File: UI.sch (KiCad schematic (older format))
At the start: 53 parts, among them Q1 2N7002BK, Q2 BS250P, U7 TXB0108

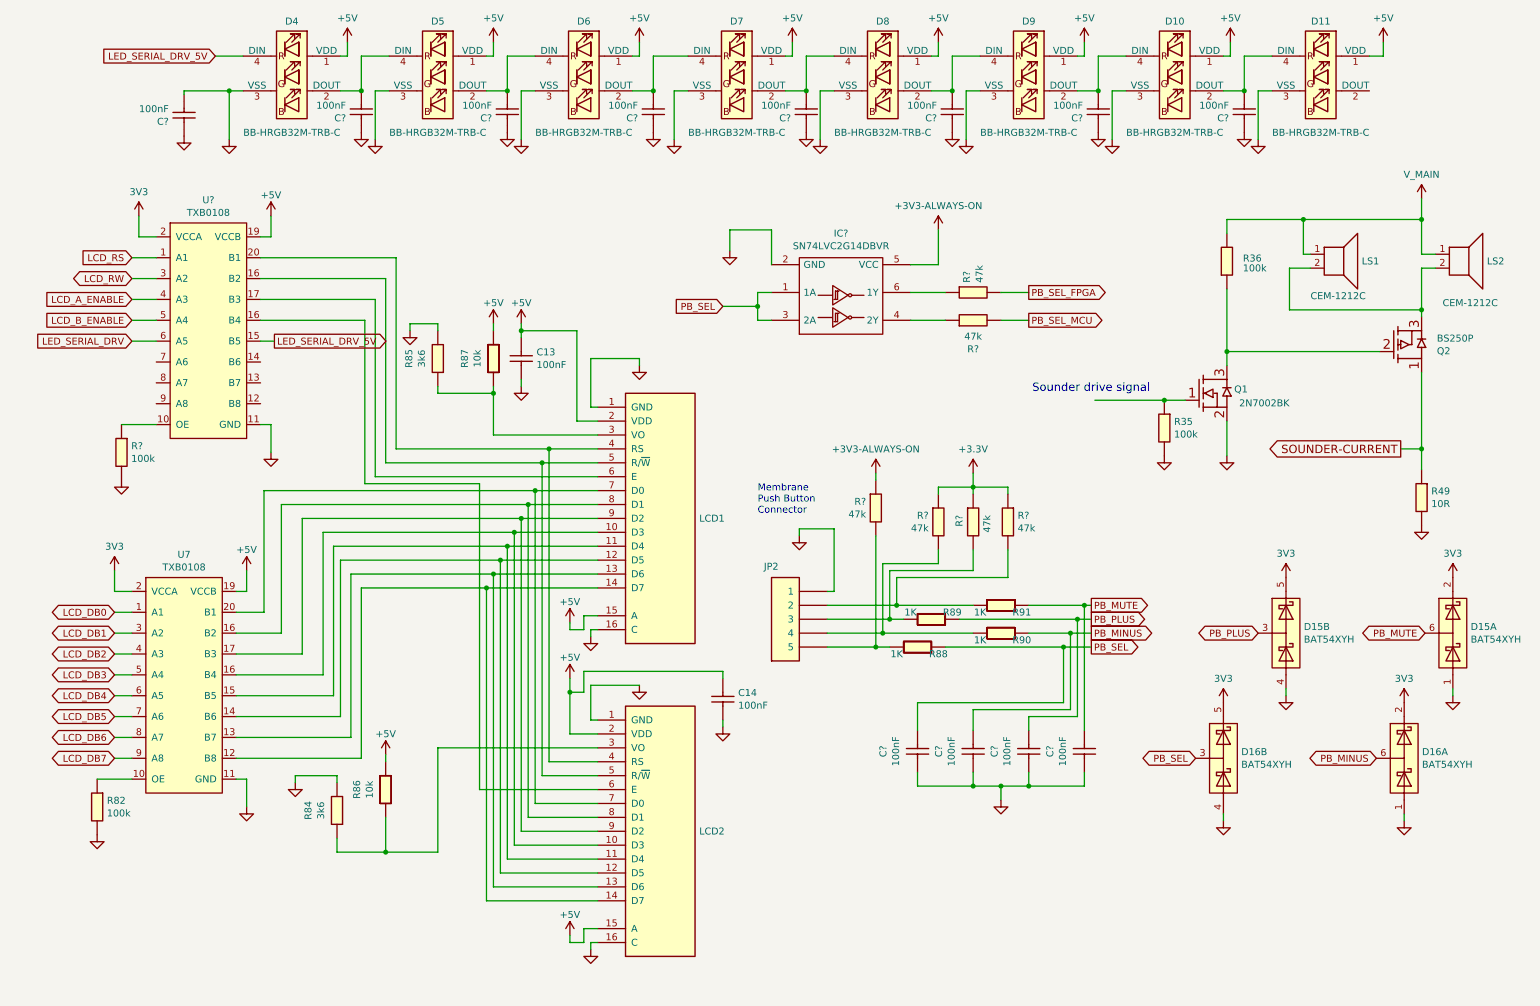
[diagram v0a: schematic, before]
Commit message: Task OEF-623
Split LCD and serial LEDs onto separate sheet as UI too full. Separated the decoupling capacitors from the serial LED for the second time to make schematic clearer. Added 74AHCT1G86 XOR gate to LED drive signal
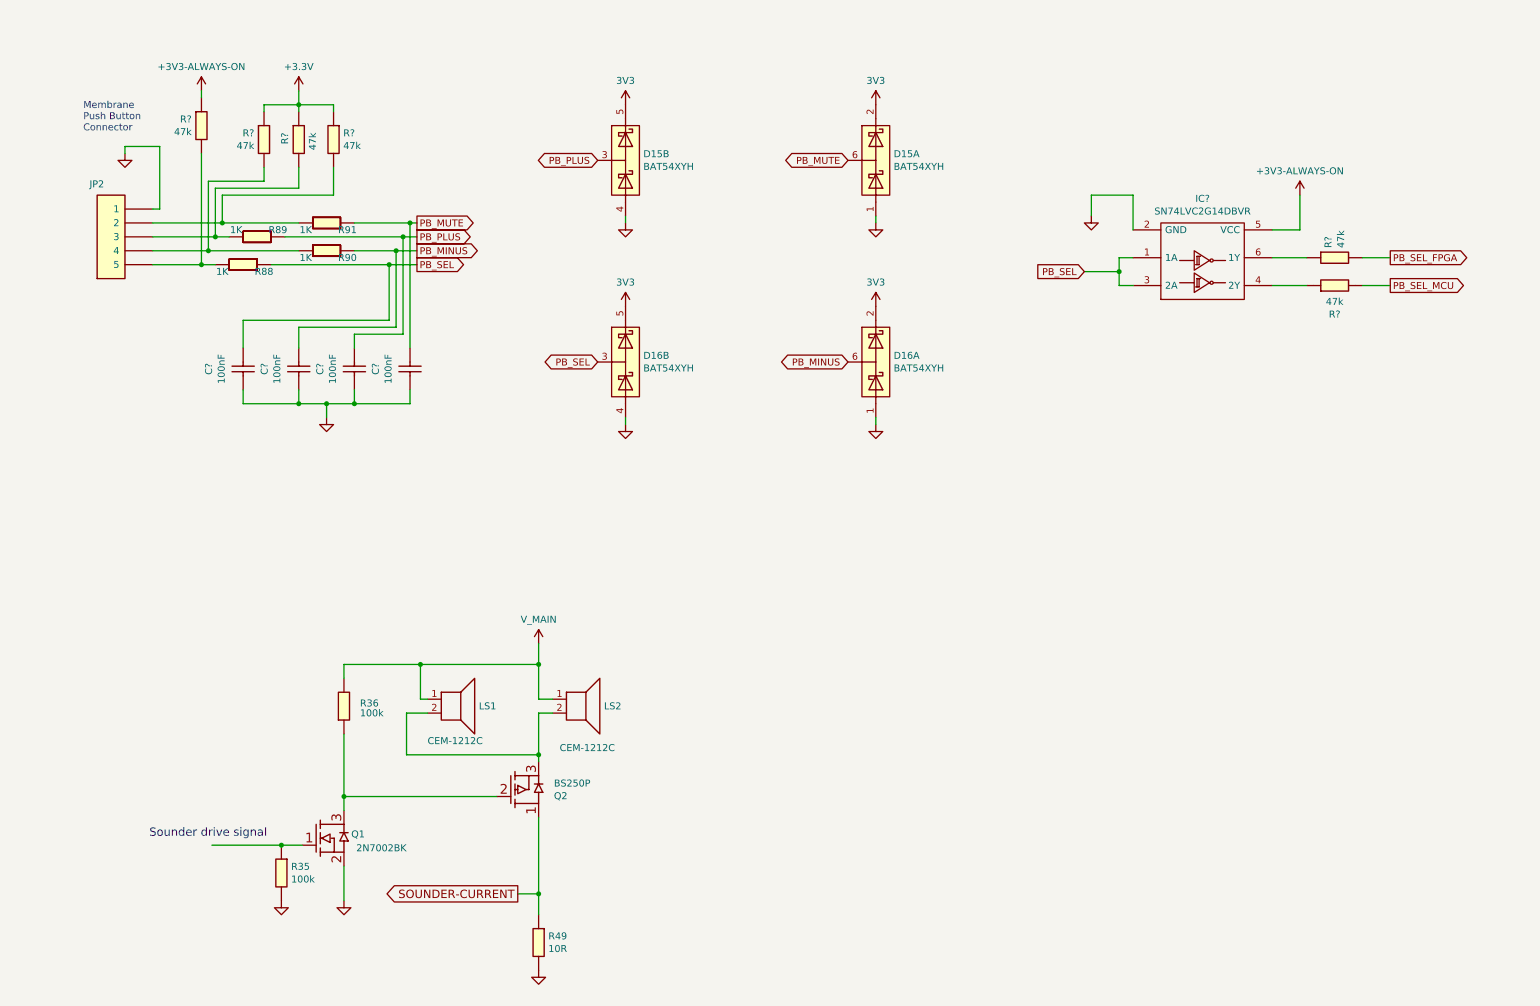
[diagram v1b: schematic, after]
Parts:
- removed C13, C14, C? (x8): 100nF_0603_Ceramic_Capacitor,_10%,_X7R,_25V, symbol OpenVent:100nF_0603_Ceramic_Capacitor,_10%,_X7R,_25V
- removed D10, D11, D4, D5, D6, D7, D8, D9: BB-HRGB32M-TRB-C, symbol OpenVent:BB-HRGB32M-TRB-C
- removed LCD1, LCD2: LCD_MOD_32DIG_16X2_TRANS_YLW_GRN, symbol OpenVent:LCD_MOD_32DIG_16X2_TRANS_YLW_GRN
- removed R82, R?: 100K_0603_Chip_Resistor,_1%,_0.1W, symbol OpenVent:100K_0603_Chip_Resistor,_1%,_0.1W
- removed R84, R85: 3k6_0603_Chip_Resistor,_1%,_0.1W, symbol OpenVent:3k6_0603_Chip_Resistor,_1%,_0.1W
- removed R86, R87: 10k_0603_Chip_Resistor,_1%,_0.1W, symbol OpenVent:10k_0603_Chip_Resistor,_1%,_0.1W
- removed U7, U?: TXB0108, symbol OpenVent:TXB0108
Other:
- moved on the sheet: C?, D15A, D15B, D16A, D16B, IC?, JP2, LS1, LS2, Q1, Q2, R35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

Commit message: Merged Rick's UI
Merged in Rick's copy of UI page (speaker circuit deleted, removing need for separate UI-visual sheet)
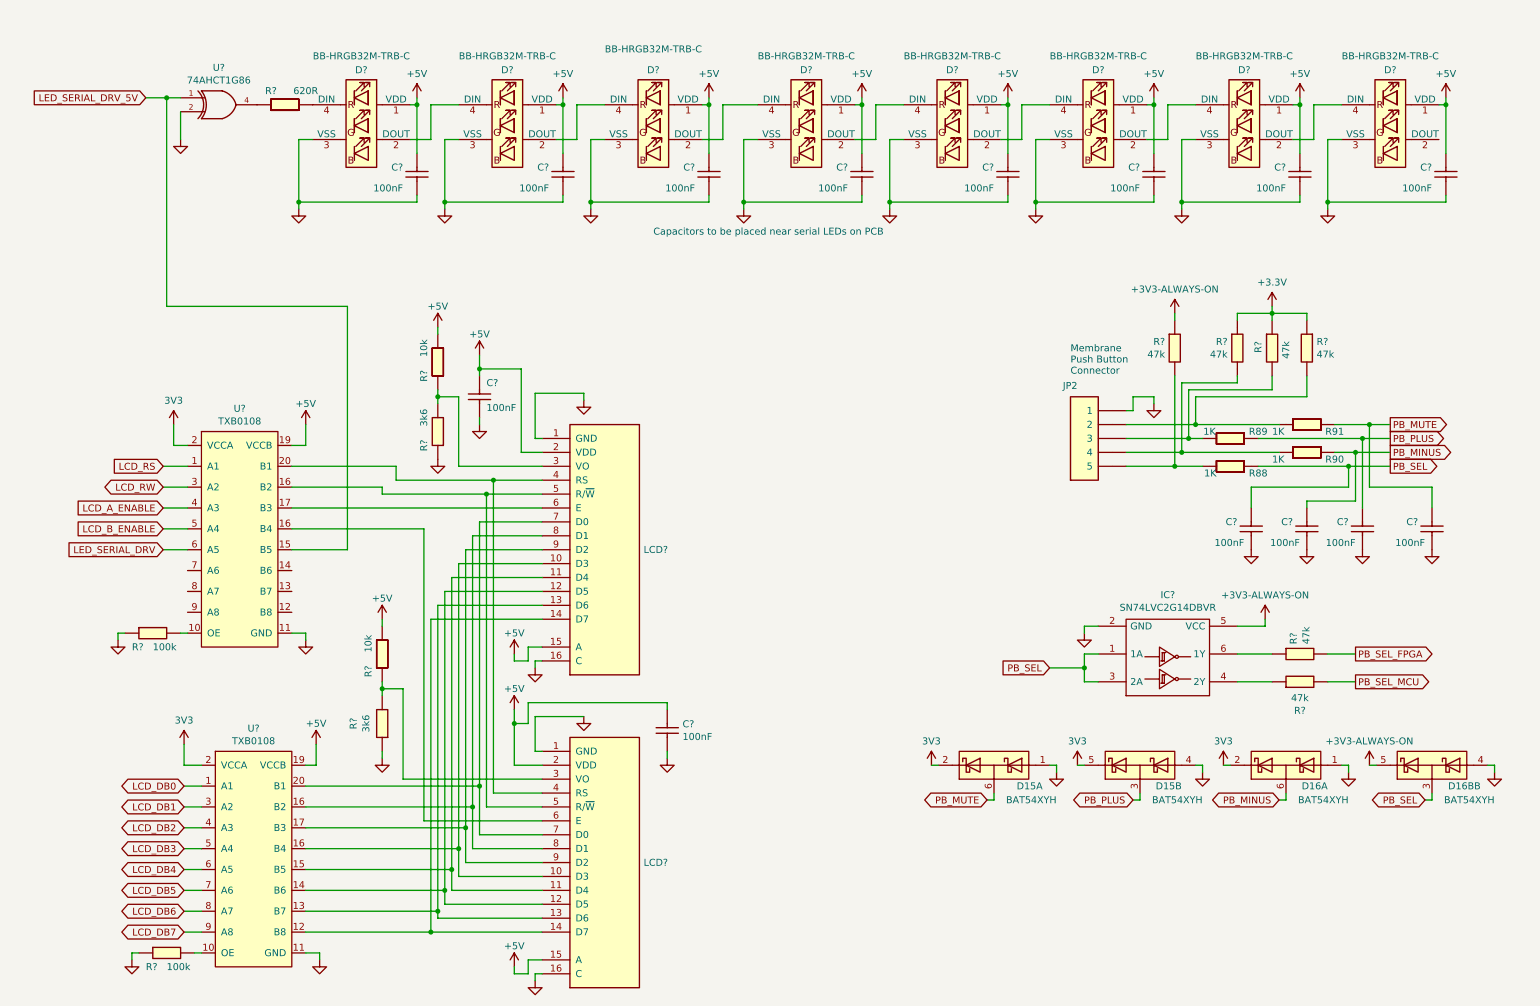
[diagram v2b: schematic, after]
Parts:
- removed C? (x4): 100nF_0603_Ceramic_Capacitor,_10%,_X7R,_25V, symbol OpenVent:100nF_0603_Ceramic_Capacitor,_10%,_X7R,_25V
- removed unit 2 of D16
- removed LS1, LS2: AUDIO_MAGNETIC_INDICATOR, Buzzer_Beeper:Buzzer_12x9.5RM7.6, symbol OpenVent-rescue:AUDIO_MAGNETIC_INDICATOR-Device
- removed Q1: 2N7002BK, Package_TO_SOT_SMD:SOT-23, symbol OpenVent:2N7002BK
- removed Q2: BS250P, symbol OpenVent:BS250P
- removed R35, R36: 100K_0603_Chip_Resistor,_1%,_0.1W, Resistor_SMD:R_0603_1608Metric, symbol OpenVent:100K_0603_Chip_Resistor,_1%,_0.1W
- removed R49: 10R_0603_Chip_Resistor,_1%,_0.1W, Resistor_SMD:R_0603_1608Metric, symbol OpenVent:10R_0603_Chip_Resistor,_1%,_0.1W
- added C? (x14): 100nF_0603_Ceramic_Capacitor,_10%,_X7R,_25V, symbol OpenVent:100nF_0603_Ceramic_Capacitor,_10%,_X7R,_25V
- added D16B: BAT54XYH, symbol OpenVent:BAT54XYH
- added D? (x8): BB-HRGB32M-TRB-C, symbol OpenVent:BB-HRGB32M-TRB-C
- added LCD? (x2): LCD_MOD_32DIG_16X2_TRANS_YLW_GRN, symbol OpenVent:LCD_MOD_32DIG_16X2_TRANS_YLW_GRN
- added R?: R_0603_620R_0.1W_1%, symbol OpenVent:R_0603_620R_0.1W_1%
- added R? (x2): 10k_0603_Chip_Resistor,_1%,_0.1W, symbol OpenVent:10k_0603_Chip_Resistor,_1%,_0.1W
- added R? (x2): 3k6_0603_Chip_Resistor,_1%,_0.1W, symbol OpenVent:3k6_0603_Chip_Resistor,_1%,_0.1W
- added R? (x2): 100K_0603_Chip_Resistor,_1%,_0.1W, symbol OpenVent:100K_0603_Chip_Resistor,_1%,_0.1W
- added U?: 74AHCT1G86, symbol OpenVent:74AHCT1G86
- added U? (x2): TXB0108, symbol OpenVent:TXB0108
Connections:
- net +3V3: now also U?.2 (VCCA), U?.2 (VCCA)
- net +5V: now also C?.1, C?.1, C?.2, C?.2, C?.2, C?.2, C?.2, C?.2, C?.2, C?.2, D?.1 (VDD), D?.1 (VDD), D?.1 (VDD), D?.1 (VDD), D?.1 (VDD), D?.1 (VDD), D?.1 (VDD), D?.1 (VDD), LCD?.15 (A), LCD?.15 (A), LCD?.2 (VDD), LCD?.2 (VDD), R?.2, R?.2, U?.19 (VCCB), U?.19 (VCCB)
- net GND: now also C?.1, C?.1, C?.1, C?.1, C?.1, C?.1, C?.1, C?.1, C?.1, C?.1, C?.1, C?.1, C?.2, C?.2, D16B.4 (A4), D?.3 (VSS), D?.3 (VSS), D?.3 (VSS), D?.3 (VSS), D?.3 (VSS), D?.3 (VSS), D?.3 (VSS), D?.3 (VSS), LCD?.1 (GND), LCD?.1 (GND), LCD?.16 (C), LCD?.16 (C), R?.1, R?.1, R?.1, R?.1, U?.11 (GND), U?.11 (GND), U?.2, U?.3 (GND)
- net PB_MINUS: now also C?.2
- net PB_MUTE: now also C?.2
- net PB_PLUS: now also C?.2
- net PB_SEL: now also C?.2, D16B.3 (A3;K4)
- net VDC: now also D16B.5 (K3)
- new net: R?.1, U?.4
- new net: D?.4 (DIN), R?.2
- new net: D?.2 (DOUT), D?.4 (DIN) (x7)
- new net: LCD?.3 (VO), R?.1, R?.2 (x2)
- new net: LCD?.10 (D3), LCD?.10 (D3), U?.16 (B4)
- new net: LCD?.11 (D4), LCD?.11 (D4), U?.15 (B5)
- new net: LCD?.12 (D5), LCD?.12 (D5), U?.14 (B6)
- new net: LCD?.13 (D6), LCD?.13 (D6), U?.13 (B7)
- new net: LCD?.14 (D7), LCD?.14 (D7), U?.12 (B8)
- new net: LCD?.4 (RS), LCD?.4 (RS), U?.20 (B1)
- new net: LCD?.5 (R/~W), LCD?.5 (R/~W), U?.16 (B4)
- new net: LCD?.6 (E), U?.17 (B3)
- new net: LCD?.7 (D0), LCD?.7 (D0), U?.20 (B1)
- new net: LCD?.8 (D1), LCD?.8 (D1), U?.16 (B4)
- new net: LCD?.9 (D2), LCD?.9 (D2), U?.17 (B3)
- new net: LCD?.6 (E), U?.16 (B4)
- new net: R?.2, U?.10 (OE) (x2)
- new net LCD_A_ENABLE: U?.4 (A3)
- new net LCD_B_ENABLE: U?.5 (A4)
- new net LCD_DB0: U?.1 (A1)
- new net LCD_DB1: U?.3 (A2)
- new net LCD_DB2: U?.4 (A3)
- new net LCD_DB3: U?.5 (A4)
- new net LCD_DB4: U?.6 (A5)
- new net LCD_DB5: U?.7 (A6)
- new net LCD_DB6: U?.8 (A7)
- new net LCD_DB7: U?.9 (A8)
- new net LCD_RS: U?.1 (A1)
- new net LCD_RW: U?.3 (A2)
- new net LED_SERIAL_DRV: U?.6 (A5)
- new net LED_SERIAL_DRV_5V: U?.1, U?.15 (B5)
- new net VCC: U?.5 (VCC)
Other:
- note added: "Capacitors to be placed near serial LEDs on PCB"
- note removed: "Sounder drive signal"
- moved on the sheet: D15B, IC?, JP2, R88, R89, R90, R91, R?

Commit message: Annotation has been done
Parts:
- gave numbers to parts that had none: 41
- renumbered D16B to D16B1
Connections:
- net GND: now also D16B1.1 (A1); no longer D16B1.4 (A4)
- net PB_SEL: now also D16B1.6 (K1;A2); no longer D16B1.3 (A3;K4)
- net VDC: now also D16B1.2 (K2); no longer D16B1.5 (K3)

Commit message: footprints
footprints added
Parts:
- D10, D3, D4, D5, D6, D7, D8, D9: footprint (none) -> OpenVent_Footprint_Test:BB-HRGB32M-TRB
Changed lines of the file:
@@
 F 0 "D4" H 3900 1800 50  0000 C CNN
 F 1 "BB-HRGB32M-TRB-C" H 3900 1900 50  0000 C CNN
-F 2 "" H 3900 1350 50  0001 C CNN
+F 2 "OpenVent_Footprint_Test:BB-HRGB32M-TRB" H 3900 1350 50  0001 C CNN
 F 3 "https://drive.google.com/file/d/1LScnK1JY8RohAoeeG1S63da97Lvbvf8K/edit" H 3900 1350 50  0001 C CNN
 	1    3900 1400
@@
 F 0 "D6" H 6050 1800 50  0000 C CNN
 F 1 "BB-HRGB32M-TRB-C" H 6050 1900 50  0000 C CNN
-F 2 "" H 6050 1350 50  0001 C CNN
+F 2 "OpenVent_Footprint_Test:BB-HRGB32M-TRB" H 6050 1350 50  0001 C CNN
 F 3 "https://drive.google.com/file/d/1LScnK1JY8RohAoeeG1S63da97Lvbvf8K/edit" H 6050 1350 50  0001 C CNN
 	1    6050 1400
@@
 F 0 "D7" H 7100 1800 50  0000 C CNN
 F 1 "BB-HRGB32M-TRB-C" H 7100 1900 50  0000 C CNN
-F 2 "" H 7100 1350 50  0001 C CNN
+F 2 "OpenVent_Footprint_Test:BB-HRGB32M-TRB" H 7100 1350 50  0001 C CNN
 F 3 "https://drive.google.com/file/d/1LScnK1JY8RohAoeeG1S63da97Lvbvf8K/edit" H 7100 1350 50  0001 C CNN
 	1    7100 1400
@@
 F 0 "D8" H 8150 1800 50  0000 C CNN
 F 1 "BB-HRGB32M-TRB-C" H 8150 1900 50  0000 C CNN
-F 2 "" H 8150 1350 50  0001 C CNN
+F 2 "OpenVent_Footprint_Test:BB-HRGB32M-TRB" H 8150 1350 50  0001 C CNN
 F 3 "https://drive.google.com/file/d/1LScnK1JY8RohAoeeG1S63da97Lvbvf8K/edit" H 8150 1350 50  0001 C CNN
 	1    8150 1400
@@
 F 0 "D9" H 9200 1800 50  0000 C CNN
 F 1 "BB-HRGB32M-TRB-C" H 9200 1900 50  0000 C CNN
-F 2 "" H 9200 1350 50  0001 C CNN
+F 2 "OpenVent_Footprint_Test:BB-HRGB32M-TRB" H 9200 1350 50  0001 C CNN
 F 3 "https://drive.google.com/file/d/1LScnK1JY8RohAoeeG1S63da97Lvbvf8K/edit" H 9200 1350 50  0001 C CNN
 	1    9200 1400
@@
 F 0 "D10" H 10250 1800 50  0000 C CNN
 F 1 "BB-HRGB32M-TRB-C" H 10250 1900 50  0000 C CNN
-F 2 "" H 10250 1350 50  0001 C CNN
+F 2 "OpenVent_Footprint_Test:BB-HRGB32M-TRB" H 10250 1350 50  0001 C CNN
 F 3 "https://drive.google.com/file/d/1LScnK1JY8RohAoeeG1S63da97Lvbvf8K/edit" H 10250 1350 50  0001 C CNN
 	1    10250 1400
@@
 F 0 "D3" H 2850 1800 50  0000 C CNN
 F 1 "BB-HRGB32M-TRB-C" H 2850 1900 50  0000 C CNN
-F 2 "" H 2850 1350 50  0001 C CNN
+F 2 "OpenVent_Footprint_Test:BB-HRGB32M-TRB" H 2850 1350 50  0001 C CNN
 F 3 "https://drive.google.com/file/d/1LScnK1JY8RohAoeeG1S63da97Lvbvf8K/edit" H 2850 1350 50  0001 C CNN
 	1    2850 1400
@@
 F 0 "D5" H 4950 1800 50  0000 C CNN
 F 1 "BB-HRGB32M-TRB-C" H 4950 1950 50  0000 C CNN
-F 2 "" H 4950 1350 50  0001 C CNN
+F 2 "OpenVent_Footprint_Test:BB-HRGB32M-TRB" H 4950 1350 50  0001 C CNN
 F 3 "https://drive.google.com/file/d/1LScnK1JY8RohAoeeG1S63da97Lvbvf8K/edit" H 4950 1350 50  0001 C CNN
 	1    4950 1400
